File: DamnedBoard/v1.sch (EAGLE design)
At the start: 20 parts, among them J1 CORTEX_DEBUG_SMD, U1 EFM32ZG108, U2 MAX44009EDT+T21-0490D-M

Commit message: V1.1 pinout with all tests points.
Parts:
- removed TP3, TP4: TEST-POINT3, SparkFun-Connectors:TEST-POINT3
- added J2: I_TEST, SparkFun-Connectors:CONN_01
- added J3: TEST, SparkFun-Connectors:CONN_02
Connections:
- net +R: now also J3.2
- net VCC: now also J2.1, U2.A0
- net VSS: now also J3.1; no longer TP3.1, TP4.1, U2.A0
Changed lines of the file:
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@@
 <part name="U$1" library="boneyard" deviceset="COPYRIGHT" device=""/>
 <part name="J1" library="SparkFun-Connectors" library_urn="urn:adsk.eagle:library:513" deviceset="CORTEX_DEBUG" device="_SMD" package3d_urn="urn:adsk.eagle:package:38289/1"/>
-<part name="TP3" library="SparkFun-Connectors" library_urn="urn:adsk.eagle:library:513" deviceset="TEST-POINT" device="3" package3d_urn="urn:adsk.eagle:package:38286/1"/>
-<part name="TP4" library="SparkFun-Connectors" library_urn="urn:adsk.eagle:library:513" deviceset="TEST-POINT" device="3" package3d_urn="urn:adsk.eagle:package:38286/1"/>
 <part name="R3" library="Seeed-Resistor" library_urn="urn:adsk.eagle:library:474" deviceset="SMD-RES-1K-5%-1/16W(0402)" device="" package3d_urn="urn:adsk.eagle:package:32792/1" value="1K"/>
 <part name="R4" library="Seeed-Resistor" library_urn="urn:adsk.eagle:library:474" deviceset="SMD-RES-1K-5%-1/16W(0402)" device="" package3d_urn="urn:adsk.eagle:package:32792/1" value="1K"/>
 <part name="TP1" library="SparkFun-Connectors" library_urn="urn:adsk.eagle:library:513" deviceset="TEST-POINT" device="3X5" package3d_urn="urn:adsk.eagle:package:38285/1"/>
 <part name="TP2" library="SparkFun-Connectors" library_urn="urn:adsk.eagle:library:513" deviceset="TEST-POINT" device="3X5" package3d_urn="urn:adsk.eagle:package:38285/1"/>
+<part name="J2" library="SparkFun-Connectors" library_urn="urn:adsk.eagle:library:513" deviceset="CONN_01" device="" package3d_urn="urn:adsk.eagle:package:38028/1" value="I_TEST"/>
+<part name="J3" library="SparkFun-Connectors" library_urn="urn:adsk.eagle:library:513" deviceset="CONN_02" device="" package3d_urn="urn:adsk.eagle:package:38039/1" value="TEST"/>
 </parts>
 <sheets>
@@
 <instance part="U$1" gate="G$1" x="48.26" y="101.6"/>
 <instance part="J1" gate="G$1" x="-25.4" y="33.02"/>
-<instance part="TP3" gate="G$1" x="68.58" y="38.1" smashed="yes" rot="R180">
-<attribute name="NAME" x="59.436" y="37.338" size="1.778" layer="95" font="vector"/>
-</instance>
-<instance part="TP4" gate="G$1" x="83.82" y="38.1" smashed="yes">
-<attribute name="NAME" x="92.964" y="38.862" size="1.778" layer="95" font="vector" rot="R180"/>
-</instance>
 <instance part="R3" gate="G$1" x="160.02" y="30.48" rot="R90"/>
 <instance part="R4" gate="G$1" x="160.02" y="7.62" rot="R90"/>
@@
 <attribute name="NAME" x="168.148" y="6.858" size="1.778" layer="95" font="vector"/>
 </instance>
+<instance part="J2" gate="G$1" x="-5.08" y="101.6"/>
+<instance part="J3" gate="G$1" x="-5.08" y="116.84"/>
 </instances>
 <busses>
@@
 <segment>
 <pinref part="U1" gate="G$1" pin="VSS"/>
-<wire x1="76.2" y1="20.32" x2="76.2" y2="38.1" width="0.1524" layer="91"/>
+<wire x1="76.2" y1="20.32" x2="76.2" y2="43.18" width="0.1524" layer="91"/>
 <pinref part="U2" gate="A" pin="GND"/>
-<wire x1="76.2" y1="38.1" x2="76.2" y2="43.18" width="0.1524" layer="91"/>
 <wire x1="88.9" y1="20.32" x2="76.2" y2="20.32" width="0.1524" layer="91"/>
-<pinref part="U2" gate="A" pin="A0"/>
-<wire x1="88.9" y1="17.78" x2="76.2" y2="17.78" width="0.1524" layer="91"/>
-<wire x1="76.2" y1="17.78" x2="76.2" y2="20.32" width="0.1524" layer="91"/>
 <junction x="76.2" y="20.32"/>
 <label x="70.358" y="28.702" size="1.778" layer="95"/>
 <pinref part="G1" gate="G$1" pin="-"/>
 <wire x1="60.96" y1="12.7" x2="76.2" y2="12.7" width="0.1524" layer="91"/>
-<wire x1="76.2" y1="12.7" x2="76.2" y2="17.78" width="0.1524" layer="91"/>
-<junction x="76.2" y="17.78"/>
-<pinref part="TP3" gate="G$1" pin="1"/>
-<wire x1="68.58" y1="38.1" x2="76.2" y2="38.1" width="0.1524" layer="91"/>
-<junction x="76.2" y="38.1"/>
-<pinref part="TP4" gate="G$1" pin="1"/>
-<wire x1="76.2" y1="38.1" x2="83.82" y2="38.1" width="0.1524" layer="91"/>
+<wire x1="76.2" y1="12.7" x2="76.2" y2="20.32" width="0.1524" layer="91"/>
 </segment>
 <segment>
@@
 <label x="-50.546" y="35.814" size="1.778" layer="95"/>
 </segment>
+<segment>
+<pinref part="J3" gate="G$1" pin="1"/>
+<wire x1="2.54" y1="116.84" x2="10.16" y2="116.84" width="0.1524" layer="91"/>
+<label x="5.588" y="117.094" size="1.778" layer="95"/>
+</segment>
 </net>
 <net name="PA0" class="0">
@@
 <label x="41.402" y="10.414" size="1.778" layer="95"/>
 </segment>
+<segment>
+<pinref part="J3" gate="G$1" pin="2"/>
+<wire x1="2.54" y1="119.38" x2="10.16" y2="119.38" width="0.1524" layer="91"/>
+<label x="5.842" y="119.888" size="1.778" layer="95"/>
+</segment>
 </net>
 <net name="+L" class="0">
@@
 <label x="160.782" y="-5.334" size="1.778" layer="95"/>
 </segment>
-</net>
+<segment>
+<pinref part="U2" gate="A" pin="A0"/>
+<wire x1="88.9" y1="17.78" x2="78.74" y2="17.78" width="0.1524" layer="91"/>
+<label x="78.994" y="18.034" size="1.778" layer="95"/>
+</segment>
+<segment>
+<pinref part="J2" gate="G$1" pin="1"/>
+<wire x1="2.54" y1="101.6" x2="10.16" y2="101.6" width="0.1524" layer="91"/>
+<label x="4.572" y="102.362" size="1.778" layer="95"/>
+</segment>
+</net>

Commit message: Progress on the adjustable version.
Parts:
- removed JP1: JUMPER-SMT_2_NC_TRACE_NO-SILK, SparkFun-Jumpers:JUMPER-SMT_2_NC_TRACE_NO-SILK
- added C3: 10nf, Seeed-Capacitor:CERAMIC-10NF-50V-10%-X7R(0402)
- added R5: PV36W104C01B00, boneyard:PV36W104C01B00
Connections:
- removed net AVDD: JP1.2, U1.AVDD_0, U1.AVDD_2
- removed net PA0: U1.PA0, U2.INT
- removed net PC0: D1.C, U1.PC0
- removed net PC1: D2.C, U1.PC1
- new net ADJ: R5.2, U1.PC1
- new net EYE_L: D1.C, U1.PA0
- new net EYE_R: D2.C, U1.PC0
- new net WAKE: U1.PF2, U2.INT
- net VCC: now also C3.2, R5.3, U1.AVDD_0, U1.AVDD_2; no longer JP1.1
- net VSS: now also C3.1, R5.1

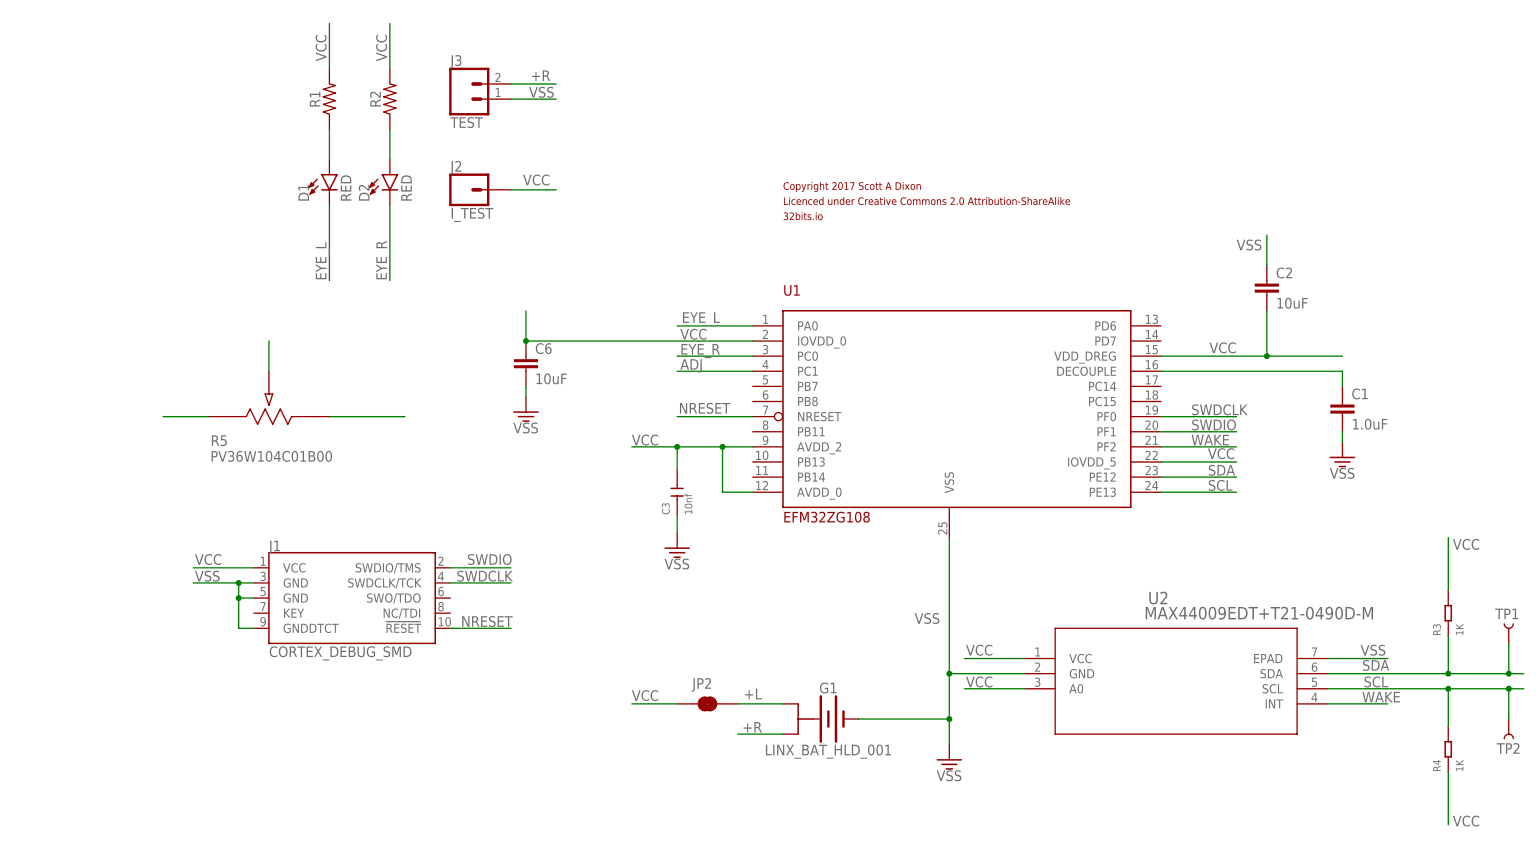
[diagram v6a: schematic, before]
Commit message: Progress on v1.1
Added trim pot to use for light threshold adjustment.
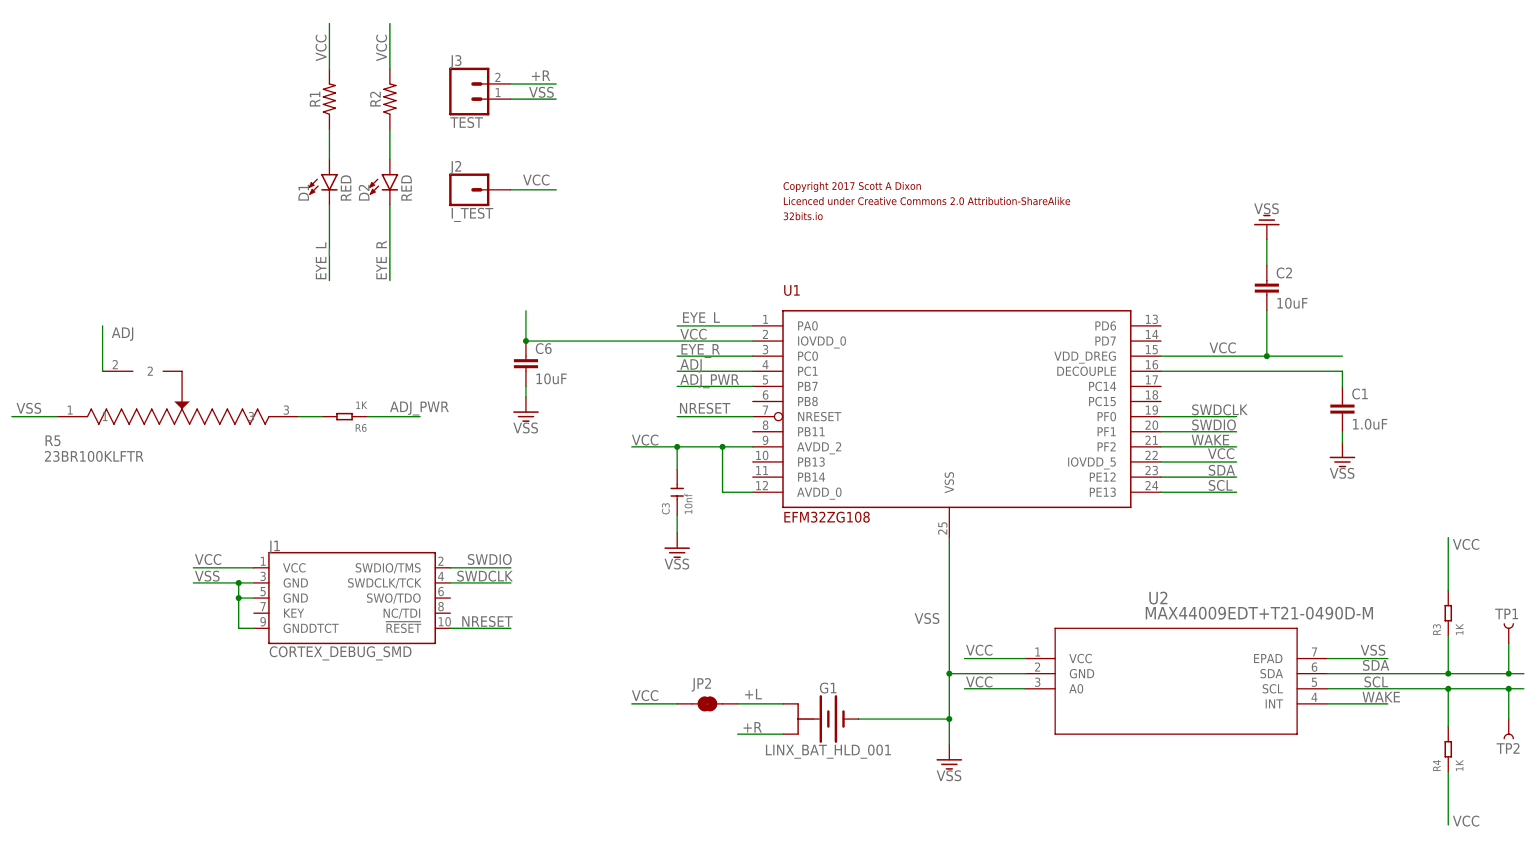
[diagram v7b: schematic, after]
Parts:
- added R6: 1K, Seeed-Resistor:SMD-RES-1K-5%-1/16W(0402)
- R5: value PV36W104C01B00 -> 23BR100KLFTR; device boneyard:PV36W104C01B00 -> boneyard:23BR100KLFTR
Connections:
- new net ADJ_PWR: R6.1, U1.PB7
- new net ADJ_PWR_SAFE: R5.3, R6.2
- net VCC: no longer R5.3
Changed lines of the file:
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@@
 <part name="J2" library="SparkFun-Connectors" library_urn="urn:adsk.eagle:library:513" deviceset="CONN_01" device="" package3d_urn="urn:adsk.eagle:package:38028/1" value="I_TEST"/>
 <part name="J3" library="SparkFun-Connectors" library_urn="urn:adsk.eagle:library:513" deviceset="CONN_02" device="" package3d_urn="urn:adsk.eagle:package:38039/1" value="TEST"/>
-<part name="R5" library="boneyard" deviceset="PV36W104C01B00" device=""/>
+<part name="R5" library="boneyard" deviceset="23BR100KLFTR" device=""/>
 <part name="C3" library="Seeed-Capacitor" library_urn="urn:adsk.eagle:library:464" deviceset="CERAMIC-10NF-50V-10%-X7R(0402)" device="" package3d_urn="urn:adsk.eagle:package:32379/1" value="10nf"/>
 <part name="VSS" library="SparkFun-PowerSymbols" library_urn="urn:adsk.eagle:library:530" deviceset="GND2" device="" value="VSS"/>
@@
 <part name="VSS2" library="SparkFun-PowerSymbols" library_urn="urn:adsk.eagle:library:530" deviceset="GND2" device="" value="VSS"/>
 <part name="VSS3" library="SparkFun-PowerSymbols" library_urn="urn:adsk.eagle:library:530" deviceset="GND2" device="" value="VSS"/>
+<part name="R6" library="Seeed-Resistor" library_urn="urn:adsk.eagle:library:474" deviceset="SMD-RES-1K-5%-1/16W(0402)" device="" package3d_urn="urn:adsk.eagle:package:32792/1" value="1K"/>
+<part name="VSS4" library="SparkFun-PowerSymbols" library_urn="urn:adsk.eagle:library:530" deviceset="GND2" device="" value="VSS"/>
 </parts>
 <sheets>
@@
 <instance part="J2" gate="G$1" x="-5.08" y="101.6"/>
 <instance part="J3" gate="G$1" x="-5.08" y="116.84"/>
-<instance part="R5" gate="A" x="-48.26" y="63.5" smashed="yes">
-<attribute name="NAME" x="-47.9044" y="58.5724" size="1.778" layer="95" ratio="10" rot="SR0"/>
-<attribute name="VALUE" x="-47.9552" y="55.9308" size="1.778" layer="96" ratio="10" rot="SR0"/>
+<instance part="R5" gate="A" x="-76.2" y="63.5" smashed="yes">
+<attribute name="NAME" x="-75.8444" y="58.5724" size="1.778" layer="95" ratio="10" rot="SR0"/>
+<attribute name="VALUE" x="-75.8952" y="55.9308" size="1.778" layer="96" ratio="10" rot="SR0"/>
 </instance>
 <instance part="C3" gate="G$1" x="30.48" y="50.8" rot="R90"/>
@@
 <instance part="VSS2" gate="G$1" x="76.2" y="5.842"/>
 <instance part="VSS3" gate="G$1" x="142.24" y="56.642"/>
+<instance part="R6" gate="G$1" x="-25.4" y="63.5" rot="R180"/>
+<instance part="VSS4" gate="G$1" x="129.54" y="95.758" rot="R180"/>
 </instances>
 <busses>
@@
 <wire x1="139.7" y1="22.86" x2="149.86" y2="22.86" width="0.1524" layer="91"/>
 <label x="145.288" y="23.368" size="1.778" layer="95"/>
-</segment>
-<segment>
-<pinref part="C2" gate="G$1" pin="1"/>
-<wire x1="129.54" y1="88.9" x2="129.54" y2="93.98" width="0.1524" layer="91"/>
-<label x="124.46" y="91.44" size="1.778" layer="95"/>
 </segment>
 <segment>
@@
 <segment>
 <pinref part="R5" gate="A" pin="1"/>
-<wire x1="-48.26" y1="63.5" x2="-55.88" y2="63.5" width="0.1524" layer="91"/>
+<wire x1="-73.66" y1="63.5" x2="-81.28" y2="63.5" width="0.1524" layer="91"/>
+<label x="-80.518" y="64.008" size="1.778" layer="95"/>
+</segment>
+<segment>
+<pinref part="C2" gate="G$1" pin="1"/>
+<pinref part="VSS4" gate="G$1" pin="3.3V"/>
+<wire x1="129.54" y1="88.9" x2="129.54" y2="93.218" width="0.1524" layer="91"/>
 </segment>
 </net>
@@
 <junction x="30.48" y="58.42"/>
 </segment>
-<segment>
-<pinref part="R5" gate="A" pin="3"/>
-<wire x1="-27.94" y1="63.5" x2="-15.24" y2="63.5" width="0.1524" layer="91"/>
-</segment>
 </net>
 <net name="WAKE" class="0">
@@
 <segment>
 <pinref part="R5" gate="A" pin="2"/>
-<wire x1="-38.1" y1="71.12" x2="-38.1" y2="76.2" width="0.1524" layer="91"/>
-</segment>
-</net>
+<wire x1="-66.04" y1="71.12" x2="-66.04" y2="78.74" width="0.1524" layer="91"/>
+<label x="-64.516" y="76.708" size="1.778" layer="95"/>
+</segment>
+</net>
+<net name="ADJ_PWR" class="0">
+<segment>
+<pinref part="U1" gate="G$1" pin="PB7"/>
+<wire x1="43.18" y1="68.58" x2="30.48" y2="68.58" width="0.1524" layer="91"/>
+<label x="30.988" y="68.834" size="1.778" layer="95"/>
+</segment>
+<segment>
+<pinref part="R6" gate="G$1" pin="1"/>
+<wire x1="-21.59" y1="63.5" x2="-12.7" y2="63.5" width="0.1524" layer="91"/>
+<label x="-17.78" y="64.262" size="1.778" layer="95"/>
+</segment>
+</net>
+<net name="ADJ_PWR_SAFE" class="0">
+<segment>
+<pinref part="R5" gate="A" pin="3"/>
+<pinref part="R6" gate="G$1" pin="2"/>
+<wire x1="-33.02" y1="63.5" x2="-29.21" y2="63.5" width="0.1524" layer="91"/>
+</segment>
+</net>

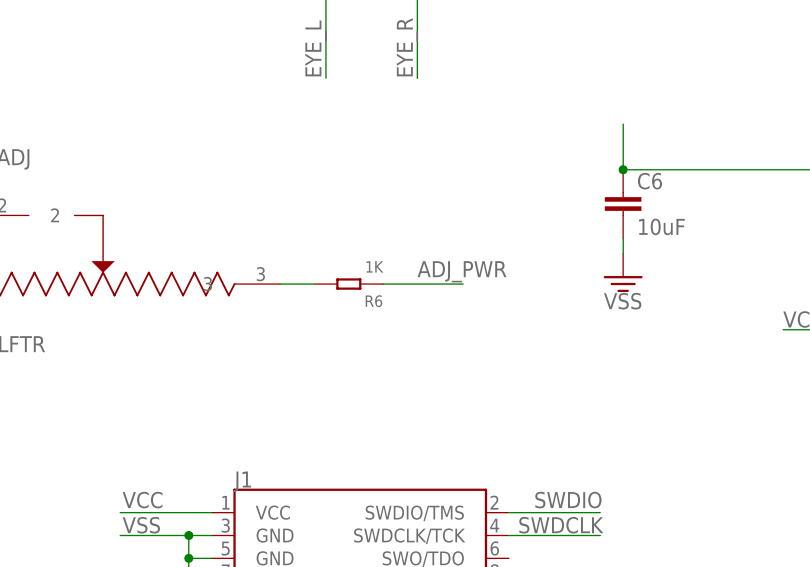
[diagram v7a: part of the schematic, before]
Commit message: Adding Yakindu machine for firmware.
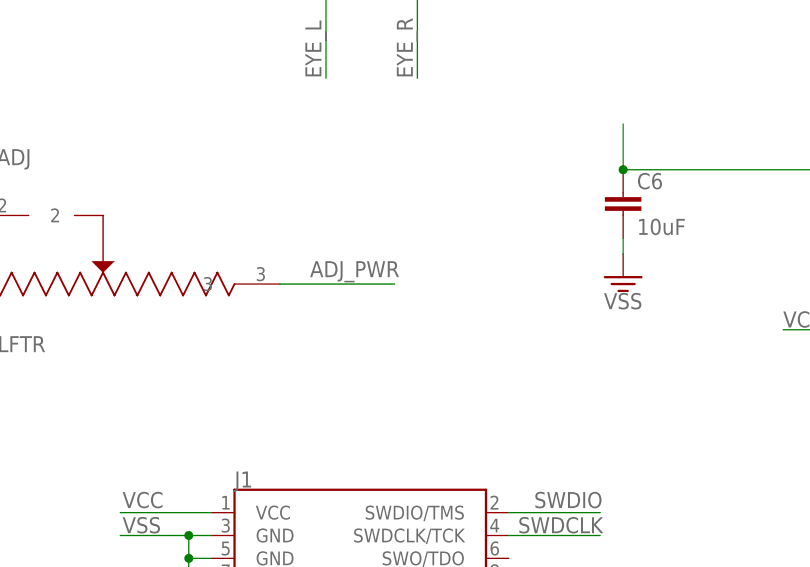
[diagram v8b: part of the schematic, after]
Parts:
- removed R6: 1K, Seeed-Resistor:SMD-RES-1K-5%-1/16W(0402)
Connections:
- removed net ADJ_PWR_SAFE: R5.3, R6.2
- net ADJ_PWR: now also R5.3; no longer R6.1
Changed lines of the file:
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@@
 <part name="VSS2" library="SparkFun-PowerSymbols" library_urn="urn:adsk.eagle:library:530" deviceset="GND2" device="" value="VSS"/>
 <part name="VSS3" library="SparkFun-PowerSymbols" library_urn="urn:adsk.eagle:library:530" deviceset="GND2" device="" value="VSS"/>
-<part name="R6" library="Seeed-Resistor" library_urn="urn:adsk.eagle:library:474" deviceset="SMD-RES-1K-5%-1/16W(0402)" device="" package3d_urn="urn:adsk.eagle:package:32792/1" value="1K"/>
 <part name="VSS4" library="SparkFun-PowerSymbols" library_urn="urn:adsk.eagle:library:530" deviceset="GND2" device="" value="VSS"/>
 </parts>
@@
 <instance part="VSS2" gate="G$1" x="76.2" y="5.842"/>
 <instance part="VSS3" gate="G$1" x="142.24" y="56.642"/>
-<instance part="R6" gate="G$1" x="-25.4" y="63.5" rot="R180"/>
 <instance part="VSS4" gate="G$1" x="129.54" y="95.758" rot="R180"/>
 </instances>
@@
 </segment>
 <segment>
-<pinref part="R6" gate="G$1" pin="1"/>
-<wire x1="-21.59" y1="63.5" x2="-12.7" y2="63.5" width="0.1524" layer="91"/>
-<label x="-17.78" y="64.262" size="1.778" layer="95"/>
-</segment>
-</net>
-<net name="ADJ_PWR_SAFE" class="0">
-<segment>
 <pinref part="R5" gate="A" pin="3"/>
-<pinref part="R6" gate="G$1" pin="2"/>
-<wire x1="-33.02" y1="63.5" x2="-29.21" y2="63.5" width="0.1524" layer="91"/>
-</segment>
-</net>
+<wire x1="-20.32" y1="63.5" x2="-33.02" y2="63.5" width="0.1524" layer="91"/>
+<label x="-29.718" y="64.262" size="1.778" layer="95"/>
+</segment>
+</net>
